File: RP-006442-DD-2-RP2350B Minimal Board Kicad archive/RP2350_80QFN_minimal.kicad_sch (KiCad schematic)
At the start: 46 parts, among them J1 USB_C_Receptacle_USB2.0_16P, J2 Conn_02x19_Odd_Even, J3 Conn_02x09_Odd_Even, SW1 SW_Push, SW2 SW_Push, U1 RP2350_80QFN, U2 NCP1117-3.3_SOT223, U3 W25Q128JVS, U4 DNF, Y1 ABM8-272-T3

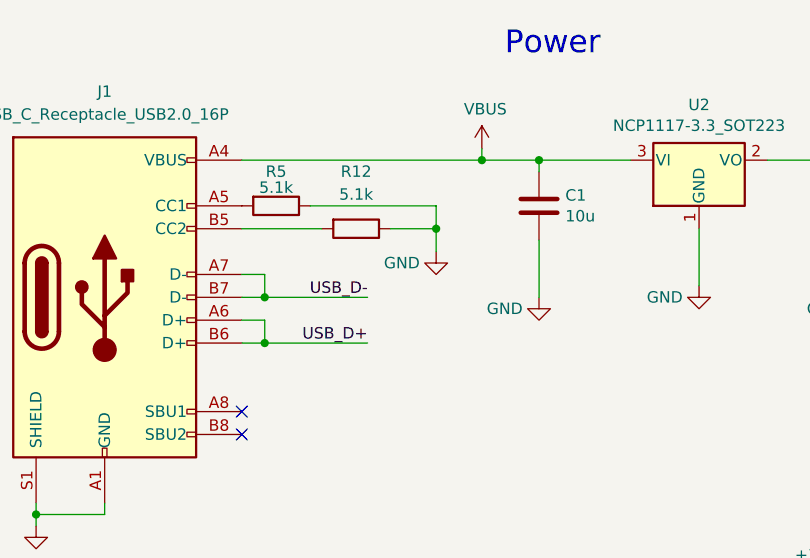
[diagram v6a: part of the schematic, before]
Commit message: Update schematic
added schottky diode to vbus on microcontroller and debug probe
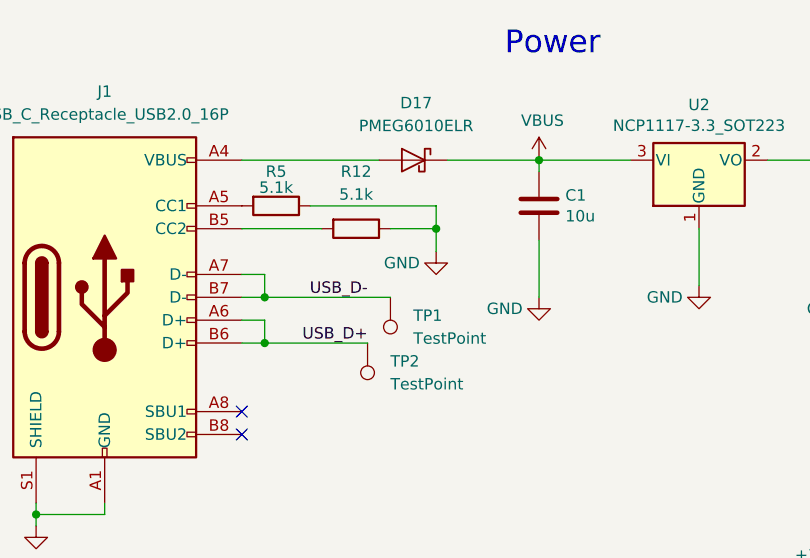
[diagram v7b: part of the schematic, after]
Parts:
- added D17: PMEG6010ELR, Diode_SMD:Nexperia_CFP3_SOD-123W, symbol Diode:PMEG6010ELR
- added TP1, TP2: TestPoint, TestPoint:TestPoint_Pad_2.0x2.0mm, symbol Connector:TestPoint
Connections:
- net USB_D+: now also TP2.1
- net USB_D-: now also TP1.1
- net VBUS: now also D17.1 (K); no longer J1.A4 (VBUS), J1.A9 (VBUS), J1.B4 (VBUS), J1.B9 (VBUS)
- new net: D17.2 (A), J1.A4 (VBUS), J1.A9 (VBUS), J1.B4 (VBUS), J1.B9 (VBUS)
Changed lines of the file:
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@@
 	)
 	(junction
-		(at 71.12 39.37)
-		(diameter 0)
-		(color 0 0 0 0)
-	)
-	(junction
 		(at 219.71 81.28)
 		(diameter 0)
@@
 	(wire
 		(pts
-			(xy 71.12 38.1) (xy 71.12 39.37)
-		)
-		(stroke
-			(width 0)
-			(type default)
-		)
-	)
-	(wire
-		(pts
 			(xy 300.99 165.1) (xy 292.1 165.1)
 		)
@@
 	(wire
 		(pts
-			(xy 46.99 54.61) (xy 58.42 54.61)
+			(xy 46.99 54.61) (xy 60.96 54.61)
 		)
 		(stroke
@@
 	(wire
 		(pts
-			(xy 71.12 39.37) (xy 77.47 39.37)
+			(xy 67.31 39.37) (xy 77.47 39.37)
 		)
 		(stroke
@@
 	(wire
 		(pts
-			(xy 241.3 95.25) (xy 241.3 101.6)
+			(xy 44.45 39.37) (xy 59.69 39.37)
 		)
 		(stroke
@@
 	(wire
 		(pts
-			(xy 44.45 39.37) (xy 71.12 39.37)
+			(xy 241.3 95.25) (xy 241.3 101.6)
 		)
 		(stroke
@@
 	(symbol
 		(lib_id "power:VBUS")
-		(at 71.12 38.1 0)
+		(at 77.47 39.37 0)
 		(unit 1)
 		(exclude_from_sim no)
@@
 		(dnp no)
 		(property "Reference" "#PWR02"
-			(at 71.12 41.91 0)
+			(at 77.47 43.18 0)
 			(effects
 				(font
@@
 		)
 		(property "Value" "VBUS"
-			(at 71.501 33.7058 0)
+			(at 77.851 34.9758 0)
 			(effects
 				(font
@@
 		)
 		(property "Footprint" ""
-			(at 71.12 38.1 0)
+			(at 77.47 39.37 0)
 			(effects
 				(font
@@
 		)
 		(property "Datasheet" ""
-			(at 71.12 38.1 0)
+			(at 77.47 39.37 0)
 			(effects
 				(font
@@
 		)
 		(property "Description" ""
-			(at 71.12 38.1 0)
+			(at 77.47 39.37 0)
 			(effects
 				(font
@@
 	)
 	(symbol
+		(lib_id "Diode:PMEG6010ELR")
+		(at 63.5 39.37 0)
+		(mirror y)
+		(unit 1)
+		(exclude_from_sim no)
+		(in_bom yes)
+		(on_board yes)
+		(dnp no)
+		(fields_autoplaced yes)
+		(property "Reference" "D17"
+			(at 63.8175 33.02 0)
+			(effects
+				(font
+					(size 1.27 1.27)
+				)
+			)
+		)
+		(property "Value" "PMEG6010ELR"
+			(at 63.8175 35.56 0)
+			(effects
+				(font
+					(size 1.27 1.27)
+				)
+			)
+		)
+		(property "Footprint" "Diode_SMD:Nexperia_CFP3_SOD-123W"
+			(at 63.5 43.815 0)
+			(effects
+				(font
+					(size 1.27 1.27)
+				)
+				(hide yes)
+			)
+		)
+		(property "Datasheet" "https://assets.nexperia.com/documents/data-sheet/PMEG6010ELR.pdf"
+			(at 63.5 39.37 0)
+			(effects
+				(font
+					(size 1.27 1.27)
+				)
+				(hide yes)
+			)
+		)
+		(property "Description" "60V, 1A low leakage current MEGA Schottky barrier rectifier, SOD-123W"
+			(at 63.5 39.37 0)
+			(effects
+				(font
+					(size 1.27 1.27)
+				)
+				(hide yes)
+			)
+		)
+		(pin "2"
+		)
+		(pin "1"
+		)
+		(instances
+			(project ""
+				(path "/94683f5c-9cd9-448e-be96-9792537b5cb8"
+					(reference "D17")
+					(unit 1)
+				)
+			)
+		)
+	)
+	(symbol
 		(lib_id "power:GND")
 		(at 74.93 173.99 0)
@@
 	)
 	(symbol
+		(lib_id "Connector:TestPoint")
+		(at 58.42 59.69 180)
+		(unit 1)
+		(exclude_from_sim no)
+		(in_bom yes)
+		(on_board yes)
+		(dnp no)
+		(fields_autoplaced yes)
+		(property "Reference" "TP2"
+			(at 60.96 61.7219 0)
+			(effects
+				(font
+					(size 1.27 1.27)
+				)
+				(justify right)
+			)
+		)
+		(property "Value" "TestPoint"
+			(at 60.96 64.2619 0)
+			(effects
+				(font
+					(size 1.27 1.27)
+				)
+				(justify right)
+			)
+		)
+		(property "Footprint" "TestPoint:TestPoint_Pad_2.0x2.0mm"
+			(at 53.34 59.69 0)
+			(effects
+				(font
+					(size 1.27 1.27)
+				)
+				(hide yes)
+			)
+		)
+		(property "Datasheet" "~"
+			(at 53.34 59.69 0)
+			(effects
+				(font
+					(size 1.27 1.27)
+				)
+				(hide yes)
+			)
+		)
+		(property "Description" "test point"
+			(at 58.42 59.69 0)
+			(effects
+				(font
+					(size 1.27 1.27)
+				)
+				(hide yes)
+			)
+		)
+		(pin "1"
+		)
+		(instances
+			(project "RP2350_80QFN_minimal"
+				(path "/94683f5c-9cd9-448e-be96-9792537b5cb8"
+					(reference "TP2")
+					(unit 1)
+				)
+			)
+		)
+	)
+	(symbol
 		(lib_name "+3V3_1")
 		(lib_id "power:+3V3")
@@
 					(unit 1)
 				)
+			)
+		)
+	)
+	(symbol
+		(lib_id "Connector:TestPoint")
+		(at 60.96 54.61 180)
+		(unit 1)
+		(exclude_from_sim no)
+		(in_bom yes)
+		(on_board yes)
+		(dnp no)
+		(fields_autoplaced yes)
+		(property "Reference" "TP1"
+			(at 63.5 56.6419 0)
+			(effects
+				(font
+					(size 1.27 1.27)
+				)
+				(justify right)
+			)
+		)
+		(property "Value" "TestPoint"
+			(at 63.5 59.1819 0)
+			(effects
+				(font
+					(size 1.27 1.27)
+				)
+				(justify right)
+			)
+		)
+		(property "Footprint" "TestPoint:TestPoint_Pad_2.0x2.0mm"
+			(at 55.88 54.61 0)
+			(effects
+				(font
+					(size 1.27 1.27)
+				)
+				(hide yes)
+			)
+		)
+		(property "Datasheet" "~"
+			(at 55.88 54.61 0)
+			(effects
+				(font
+					(size 1.27 1.27)
+				)
+				(hide yes)
+			)
+		)
+		(property "Description" "test point"
+			(at 60.96 54.61 0)
+			(effects
+				(font
+					(size 1.27 1.27)
+				)
+				(hide yes)
+			)
+		)
+		(pin "1"
+		)
+		(instances
+			(project ""
+				(path "/94683f5c-9cd9-448e-be96-9792537b5cb8"
+					(reference "TP1")
+					(unit 1)
+				)
